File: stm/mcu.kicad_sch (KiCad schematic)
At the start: 47 parts, among them J1 Conn_02x07_Odd_Even, J2 SD_Card_Receptacle, SW2 SW_Push, U1 REF4132B25DBVR, U2 STM32H730ZBTx, U6 MAX13448EESD_, Y3 25MHz, Y4 ABS05-32.768KHZ-T

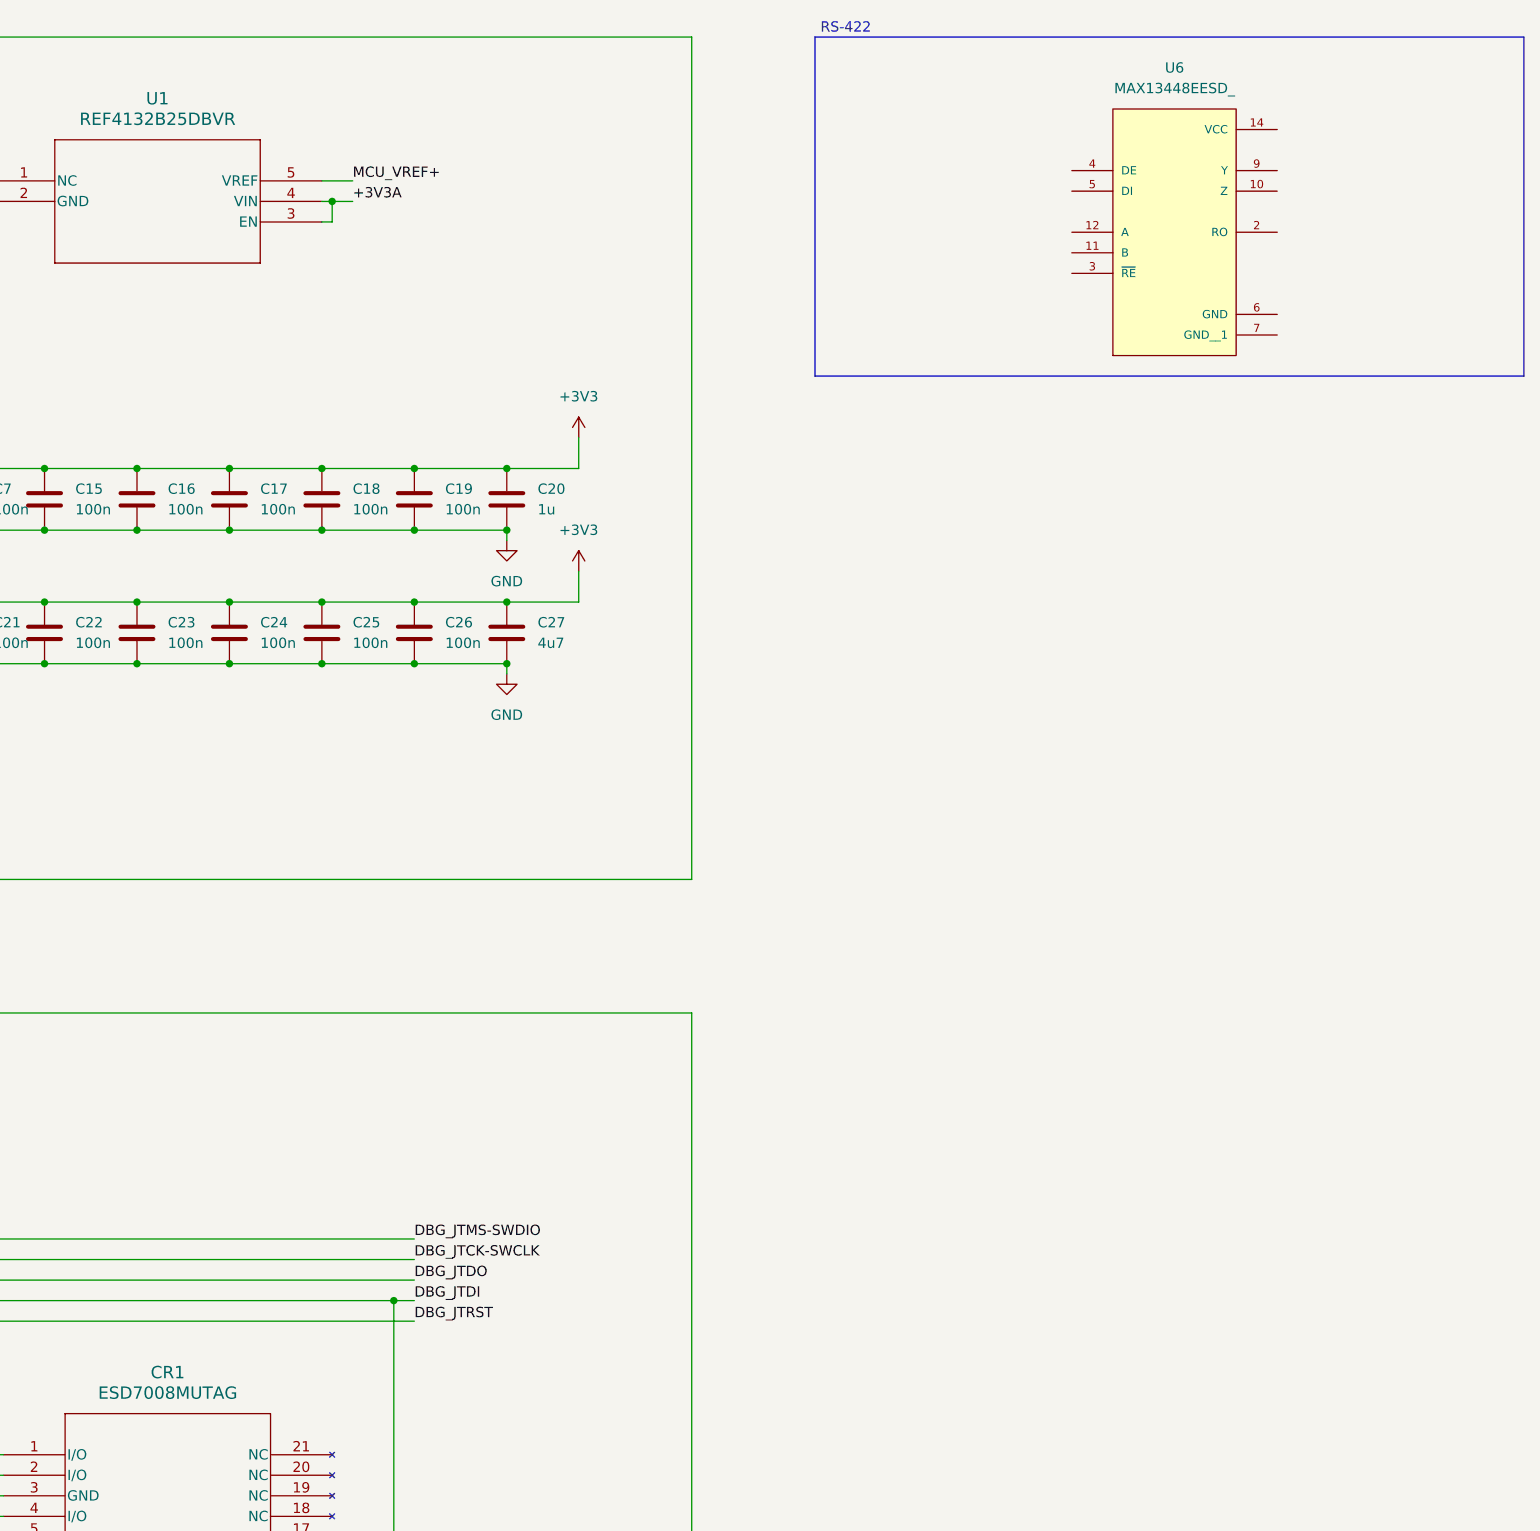
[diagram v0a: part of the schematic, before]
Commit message: Added components to main libs folder
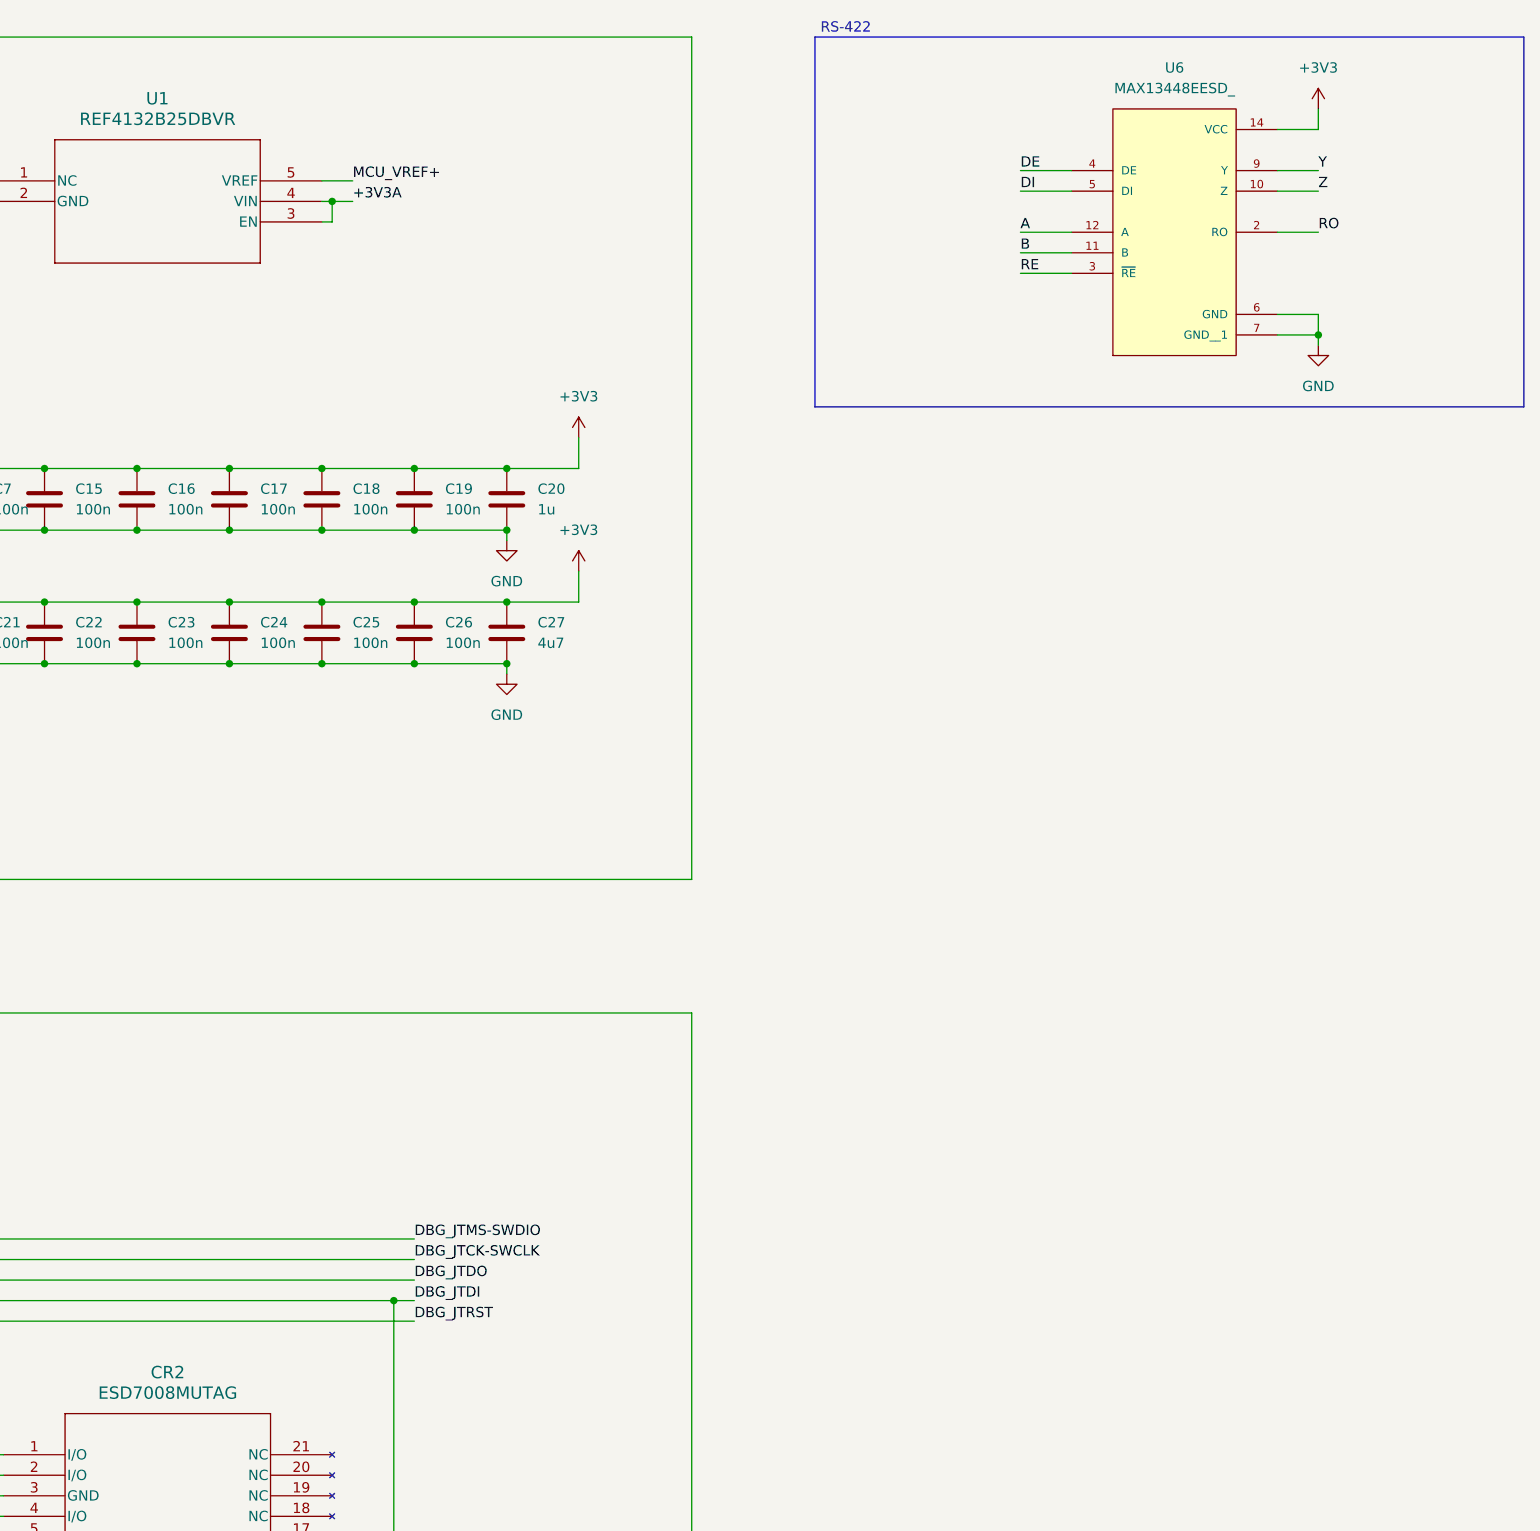
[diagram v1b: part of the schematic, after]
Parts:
- removed CR1: ESD7008MUTAG, symbol ESD7008MUTAG:ESD7008MUTAG
- added CR2: ESD7008MUTAG, ESD7008MUTAG:UDFN18_517BV_ONS, symbol ESD7008MUTAG:ESD7008MUTAG
- C1, C10, C11, C12, C13, C14, C15, C16, C17, C18, C19, C2, C20, C21, C22, C23, C24, C25, C26, C27, C3, C4, C5, C7, C8, C9: footprint (none) -> Capacitor_SMD:C_0603_1608Metric
- R10, R11, R2, R3, R4, R5, R6, R7, R8, R9: footprint (none) -> Resistor_SMD:R_0603_1608Metric
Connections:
- net +3V3: now also U6.14 (VCC), CR2.5 (I/O)
- net DBG_JTCK-SWCLK: now also CR2.8 (I/O)
- net DBG_JTDI: now also CR2.11 (I/O)
- net DBG_JTDO: now also CR2.10 (I/O)
- net DBG_JTMS-SWDIO: now also CR2.7 (I/O)
- net DBG_JTRST: now also CR2.1 (I/O)
- net GND: now also U6.6 (GND), U6.7 (GND__1), CR2.13 (GND), CR2.15 (GND), CR2.17 (GND), CR2.3 (GND), CR2.6 (GND), CR2.9 (GND)
- net at J1.14 (Pin_14): now also CR2.2 (I/O)
- net at J1.13 (Pin_13): now also CR2.4 (I/O)
- net Z: now reaches U6.10 (Z)
- net B: now reaches U6.11 (B)
- net A: now reaches U6.12 (A)
- net RO: now reaches U6.2 (RO)
- net RE: now reaches U6.3 (~{RE})
- net DE: now reaches U6.4 (DE)
- net DI: now reaches U6.5 (DI)
- net Y: now reaches U6.9 (Y)
